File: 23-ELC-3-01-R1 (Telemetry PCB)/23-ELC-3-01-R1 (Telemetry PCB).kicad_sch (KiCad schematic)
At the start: 28 parts, among them J101 SPRINKLES Harness, J102 GLV Harness, J103 Serial Radio, J104 Raspberry_Pi_4b, J105 Conn_01x01, J106 Fan Header, U101 DS3231M, U103 Adafruit_Ultimate_GPS_V3

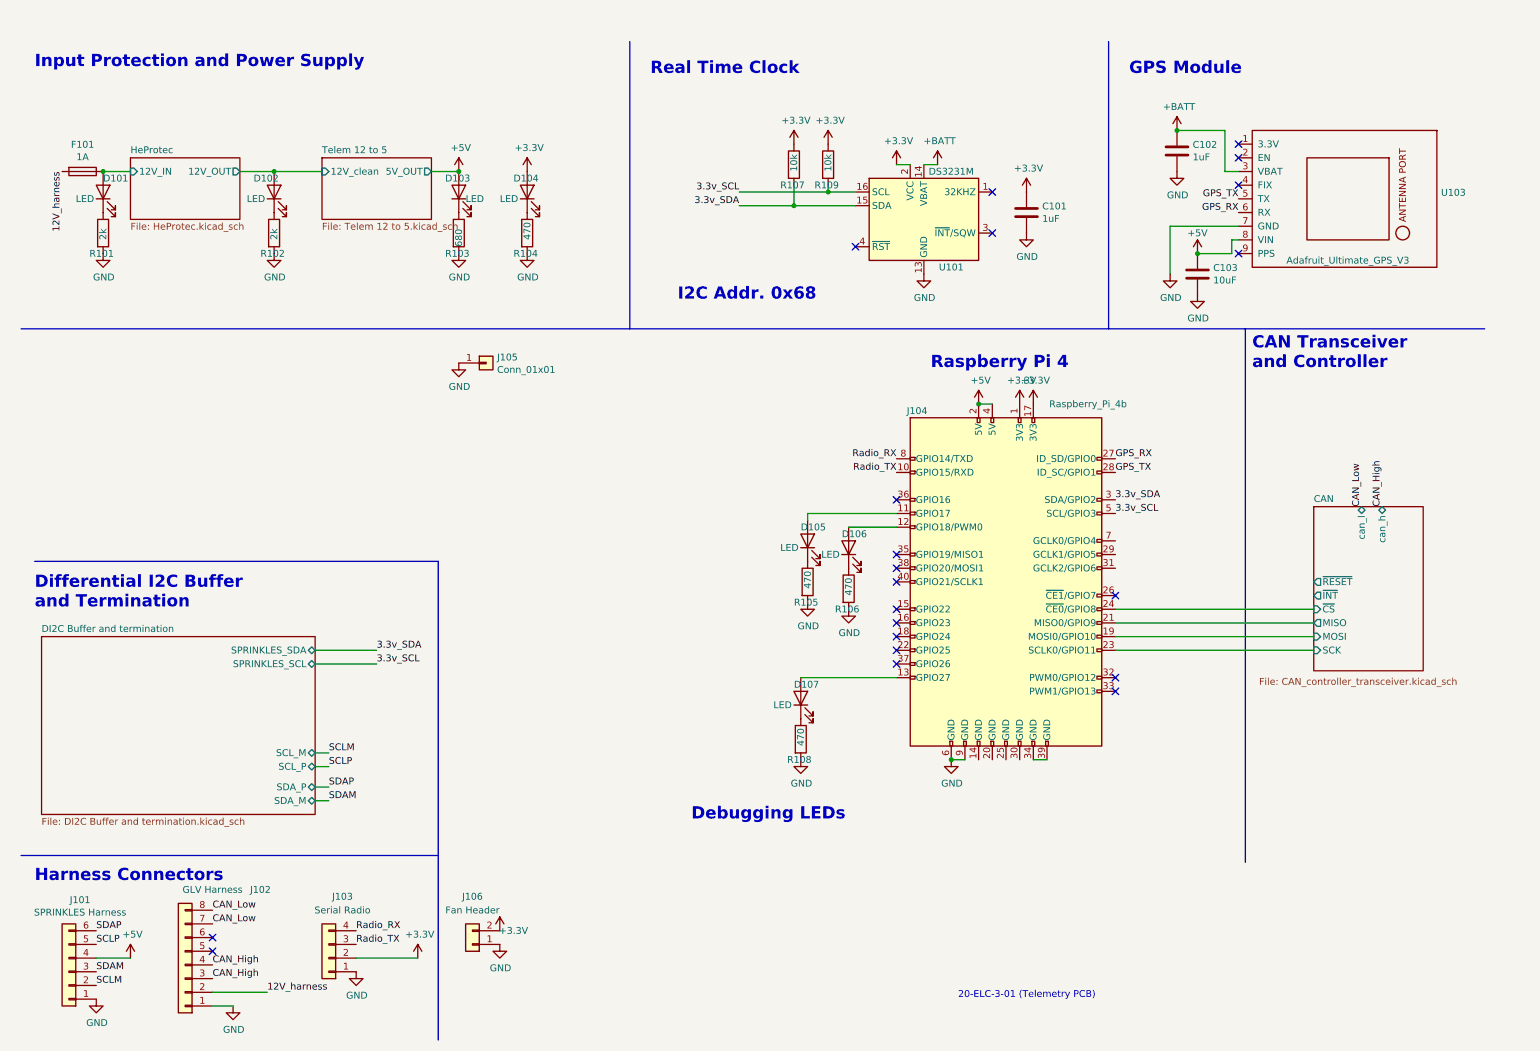
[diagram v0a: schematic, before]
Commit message: Added some CAN hardware
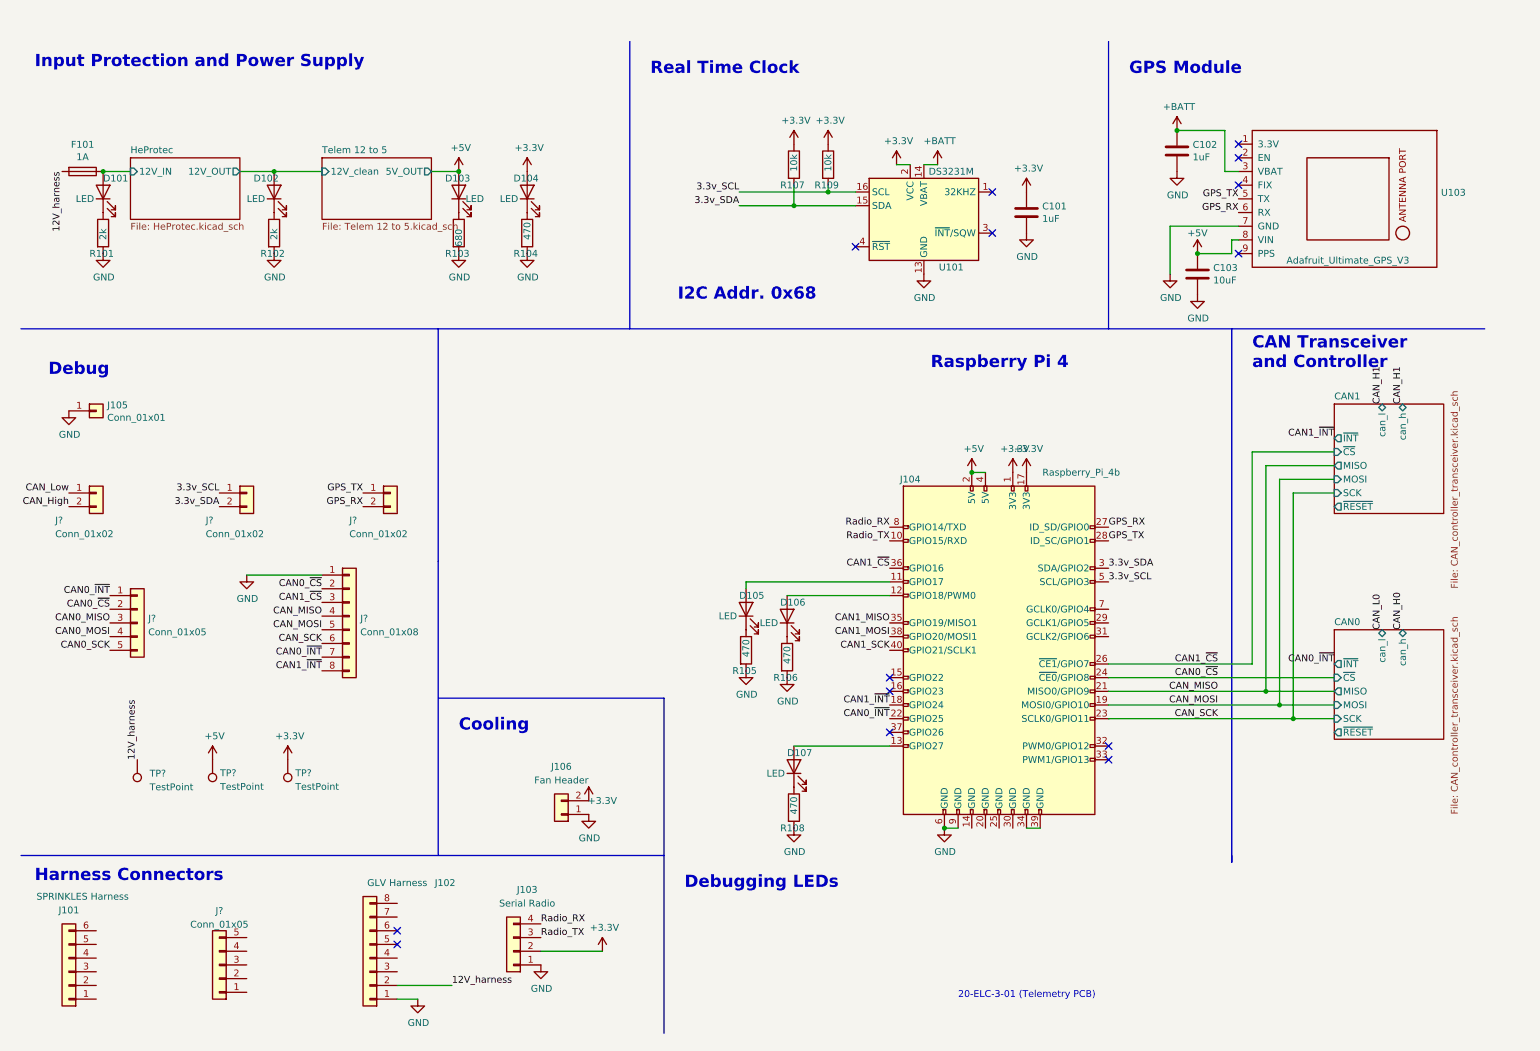
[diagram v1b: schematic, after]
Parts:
- added J? (x3): Conn_01x02, Connector_PinHeader_2.54mm:PinHeader_1x02_P2.54mm_Vertical, symbol Connector_Generic:Conn_01x02
- added J?: Conn_01x05, symbol Connector_Generic:Conn_01x05
- added J?: Conn_01x08, symbol Connector_Generic:Conn_01x08
- added J?: Conn_01x05, Connector_PinHeader_1.00mm:PinHeader_1x05_P1.00mm_Vertical, symbol Connector_Generic:Conn_01x05
- added TP? (x3): TestPoint, TestPoint:TestPoint_Keystone_5005-5009_Compact, symbol Connector:TestPoint
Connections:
- net +3V3: now also TP?.1
- net +5V: now also TP?.1; no longer J101.4 (Pin_4)
- net 12V_harness: now also TP?.1
- net 3.3v_SCL: now also J?.1 (Pin_1)
- net 3.3v_SDA: now also J?.2 (Pin_2)
- net CAN_High: now also J?.2 (Pin_2); no longer J102.3 (Pin_3), J102.4 (Pin_4)
- net CAN_Low: now also J?.1 (Pin_1); no longer J102.7 (Pin_7), J102.8 (Pin_8)
- net GND: now also J?.1 (Pin_1); no longer J101.1 (Pin_1)
- net GPS_RX: now also J?.2 (Pin_2)
- net GPS_TX: now also J?.1 (Pin_1)
- net CAN1_~{INT}: now reaches J104.18 (GPIO24)
- net CAN1_~{INT}: now also J?.8 (Pin_8)
- net CAN0_~{INT}: now reaches J104.22 (GPIO25)
- net CAN0_~{INT}: now also J?.1 (Pin_1), J?.7 (Pin_7)
- net CAN1_~{CS}: now reaches J104.26 (~{CE1}/GPIO7)
- net CAN1_~{CS}: now also J104.36 (GPIO16), J?.3 (Pin_3)
- net CAN1_MISO: now reaches J104.35 (GPIO19/MISO1)
- net CAN1_MOSI: now reaches J104.38 (GPIO20/MOSI1)
- net CAN1_SCK: now reaches J104.40 (GPIO21/SCLK1)
- net CAN0/MISO renamed CAN_MISO
- net CAN_MISO: now also J?.4 (Pin_4)
- net CAN0/MOSI renamed CAN_MOSI
- net CAN_MOSI: now also J?.5 (Pin_5)
- net CAN0/SCK renamed CAN_SCK
- net CAN_SCK: now also J?.6 (Pin_6)
- net CAN0/~{CS} renamed CAN0_~{CS}
- net CAN0_~{CS}: now also J?.2 (Pin_2), J?.2 (Pin_2)
- net SCLM: no longer names the net of J101.2 (Pin_2)
- net SCLP: no longer names the net of J101.5 (Pin_5)
- net SDAM: no longer names the net of J101.3 (Pin_3)
- net SDAP: no longer names the net of J101.6 (Pin_6)
- new net CAN0_MISO: J?.3 (Pin_3)
- new net CAN0_MOSI: J?.4 (Pin_4)
- new net CAN0_SCK: J?.5 (Pin_5)
- no-connect marks 21 -> 14
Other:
- sheet CAN renamed CAN0
- removed sheet DI2C Buffer and termination
- added sheet CAN1 (CAN_controller_transceiver.kicad_sch)
- note added: "Cooling"
- note added: "Debug"
- note removed: "Differential I2C Buffer and Termination"
- moved on the sheet: D105, D106, D107, J102, J103, J104, J105, J106, R105, R106, R108

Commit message: Finished CAN circuits probably
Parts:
- removed C102: 1uF, Capacitor_SMD:C_0805_2012Metric_Pad1.15x1.40mm_HandSolder, symbol Device:C
- removed C103: 10uF, Capacitor_SMD:C_0805_2012Metric_Pad1.15x1.40mm_HandSolder, symbol Device:C
- removed D105, D106: LED, LED_SMD:LED_0603_1608Metric_Pad1.05x0.95mm_HandSolder, symbol Device:LED
- removed J? (x2): Conn_01x02, Connector_PinHeader_2.54mm:PinHeader_1x02_P2.54mm_Vertical, symbol Connector_Generic:Conn_01x02
- removed J?: Conn_01x05, symbol Connector_Generic:Conn_01x05
- removed J?: Conn_01x08, symbol Connector_Generic:Conn_01x08
- removed J?: Conn_01x05, Connector_PinHeader_1.00mm:PinHeader_1x05_P1.00mm_Vertical, symbol Connector_Generic:Conn_01x05
- removed R105, R106: 470, Resistor_SMD:R_0603_1608Metric_Pad1.05x0.95mm_HandSolder, symbol Device:R
- removed U103: Adafruit_Ultimate_GPS_V3, LHRE Footprint Library:Adafruit_Ultimate_GPS_V3, symbol LHRE_Component_Library:Adafruit_Ultimate_GPS_V3
- added J? (x3): Conn_01x02, Connector_PinHeader_2.54mm:PinHeader_1x02_P2.54mm_Vertical, symbol Connector_Generic:Conn_01x02
- added J? (x2): Conn_01x08, symbol Connector_Generic:Conn_01x08
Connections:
- net CAN1_~{CS}: no longer J104.26 (~{CE1}/GPIO7)
- net GND: now also J?.1 (Pin_1), J?.1 (Pin_1)
- net CAN_CS_3: now reaches J104.11 (GPIO17)
- net CAN_CS_3: now also J?.8 (Pin_8)
- net CAN_CS_2: now reaches J104.12 (GPIO18/PWM0)
- net CAN_CS_2: now also J?.6 (Pin_6)
- net CAN_INT_0: now reaches J104.15 (GPIO22)
- net CAN_INT_0: now also J?.5 (Pin_5)
- net CAN_INT_1: now reaches J104.16 (GPIO23)
- net CAN_INT_1: now also J?.7 (Pin_7)
- net CAN0_~{CS} renamed CAN_CS_0
- net CAN_CS_0: now also J?.6 (Pin_6)
- net CAN0_~{INT} renamed CAN_INT_3
- net CAN_INT_3: now also J?.7 (Pin_7)
- net CAN1_MISO renamed CAN_MISO_23
- net CAN_MISO_23: now also J?.2 (Pin_2)
- net CAN1_MOSI renamed CAN_MOSI_23
- net CAN_MOSI_23: now also J?.3 (Pin_3)
- net CAN1_SCK renamed CAN_SCK_23
- net CAN_SCK_23: now also J?.4 (Pin_4)
- net CAN1_~{INT} renamed CAN_INT_2
- net CAN_INT_2: now also J?.5 (Pin_5)
- net CAN_High renamed CAN_H_0
- net CAN_Low renamed CAN_L_0
- net CAN_MISO renamed CAN_MISO_01
- net CAN_MISO_01: now also J?.2 (Pin_2)
- net CAN_MOSI renamed CAN_MOSI_01
- net CAN_MOSI_01: now also J?.3 (Pin_3)
- net CAN_SCK renamed CAN_SCK_01
- net CAN_SCK_01: now also J?.4 (Pin_4)
- net GPS_RX: no longer names the net of J104.27 (ID_SD/GPIO0)
- net GPS_TX: no longer names the net of J104.28 (ID_SC/GPIO1)
- new net CAN_CS_1: J104.26 (~{CE1}/GPIO7), J?.8 (Pin_8)
- new net CAN_H_1: J?.2 (Pin_2)
- new net CAN_H_2: J?.2 (Pin_2)
- new net CAN_H_3: J?.2 (Pin_2)
- new net CAN_L_1: J?.1 (Pin_1)
- new net CAN_L_2: J?.1 (Pin_1)
- new net CAN_L_3: J?.1 (Pin_1)
- no-connect marks 14 -> 10
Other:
- added sheet CAN2 (CAN_controller_transceiver.kicad_sch)
- added sheet CAN3 (CAN_controller_transceiver.kicad_sch)
- note added: "TODO: 24V power New protection circuit Harness connectors Verify RTC"
- note removed: "Debugging LEDs"
- note removed: "GPS Module"
- moved on the sheet: D107, J?, R108

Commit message: Ready for review
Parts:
- removed C101: 1uF, Capacitor_SMD:C_0805_2012Metric_Pad1.15x1.40mm_HandSolder, symbol Device:C
- removed D102: LED, LED_SMD:LED_0603_1608Metric_Pad1.05x0.95mm_HandSolder, symbol Device:LED
- removed J101: SPRINKLES Harness, Connector_Molex:Molex_Micro-Fit_3.0_43045-0600_2x03_P3.00mm_Horizontal, symbol Connector_Generic:Conn_01x06
- removed J102: GLV Harness, Connector_Molex:Molex_Micro-Fit_3.0_43045-0800_2x04_P3.00mm_Horizontal, symbol Connector_Generic:Conn_01x08
- removed J103: Serial Radio, Connector_Molex:Molex_Micro-Fit_3.0_43045-0400_2x02_P3.00mm_Horizontal, symbol Connector_Generic:Conn_01x04
- removed R102: 2k, Resistor_SMD:R_0603_1608Metric_Pad1.05x0.95mm_HandSolder, symbol Device:R
- removed R107, R109: 10k, Resistor_SMD:R_0603_1608Metric_Pad1.05x0.95mm_HandSolder, symbol Device:R
- removed U101: DS3231M, Package_SO:SOIC-16W_7.5x10.3mm_P1.27mm, symbol Timer_RTC:DS3231M
- added J10: Conn_02x12_Top_Bottom, Global Libraries:DRC23-24PB, symbol Connector_Generic:Conn_02x12_Top_Bottom
- added J?: DS3231, Connector_PinHeader_2.54mm:PinHeader_1x06_P2.54mm_Vertical, symbol Connector_Generic:Conn_01x06
- added J?: Conn_01x04, Connector_Molex:Molex_Micro-Fit_3.0_43045-0400_2x02_P3.00mm_Horizontal, symbol Connector_Generic:Conn_01x04
- added SW? (x2): SW_DPDT_x2, symbol Switch:SW_DPDT_x2
- added TP1: TestPoint, TestPoint:TestPoint_Keystone_5005-5009_Compact, symbol Connector:TestPoint
- R101: value 2k -> 3.3k
- gave numbers to parts that had none: 9
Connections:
- net +3V3: now also J?.5 (Pin_5)
- net 12V_harness: no longer F101.2
- net 3.3v_SCL: now also J?.3 (Pin_3)
- net 3.3v_SDA: now also J?.4 (Pin_4)
- net CAN_H_0: now also J10.2 (Pin_2), J10.8 (Pin_8)
- net CAN_H_1: now also SW?.2 (B)
- net CAN_H_2: now also J10.11 (Pin_11), J10.17 (Pin_17)
- net CAN_H_3: now also J10.23 (Pin_23)
- net CAN_L_0: now also J10.3 (Pin_3), J10.9 (Pin_9)
- net CAN_L_1: now also SW?.5 (B)
- net CAN_L_2: now also J10.12 (Pin_12), J10.18 (Pin_18)
- net CAN_L_3: now also J10.24 (Pin_24)
- net GND: now also J10.1 (Pin_1), J10.7 (Pin_7), J?.1 (Pin_1), J?.6 (Pin_6), TP1.1
- net HeProtec/12V_IN renamed Buck 24 to 5/V_in
- net Radio_RX: no longer names the net of J104.8 (GPIO14/TXD)
- net Radio_TX: no longer names the net of J104.10 (GPIO15/RXD)
- new net +24V: F101.2, J10.19 (Pin_19)
- new net CAN_H_1_A: J10.14 (Pin_14), J10.20 (Pin_20), SW?.1 (A)
- new net CAN_H_1_B: J10.5 (Pin_5), SW?.3 (C)
- new net CAN_L_1_A: J10.15 (Pin_15), J10.21 (Pin_21), SW?.4 (A)
- new net CAN_L_1_B: J10.6 (Pin_6), SW?.6 (C)
- new net TSAL_G: J10.4 (Pin_4), J?.2 (Pin_2)
- new net TSAL_R: J10.10 (Pin_10), J?.3 (Pin_3)
- no-connect marks 10 -> 9
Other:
- removed sheet HeProtec
- removed sheet Telem 12 to 5
- added sheet Buck 24 to 5 (..\2023KicadLibrary\Standardized Subsheets\BUCK.kicad_sch)
- note added: "32K SQW SCL SDA 3V3 GND"
- note added: "CAN0 - Telemetry CAN1A - IVTS/Dash CAN1B - User CAN2 - Inv/Dash CAN3 - BMS"
- note added: "Using DS3231 breakout board Can find online or on Amazon from several companies"
- note removed: "TODO: 24V power New protection circuit Harness connectors Verify RTC"
- moved on the sheet: D103, D107, J104, J106, R103, R108
